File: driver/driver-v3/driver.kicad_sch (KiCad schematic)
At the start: 40 parts, among them J1 Conn_02x08_Odd_Even_Male, J2 Conn_02x08_Odd_Even_Female, J3 Conn_01x05, J4 Conn_01x03_Pin, J5 Conn_01x05, J6 Conn_01x03_Pin, U1 DRV8804PWP, U2 SN74HCS165DYYR, U3 DRV8804PWP

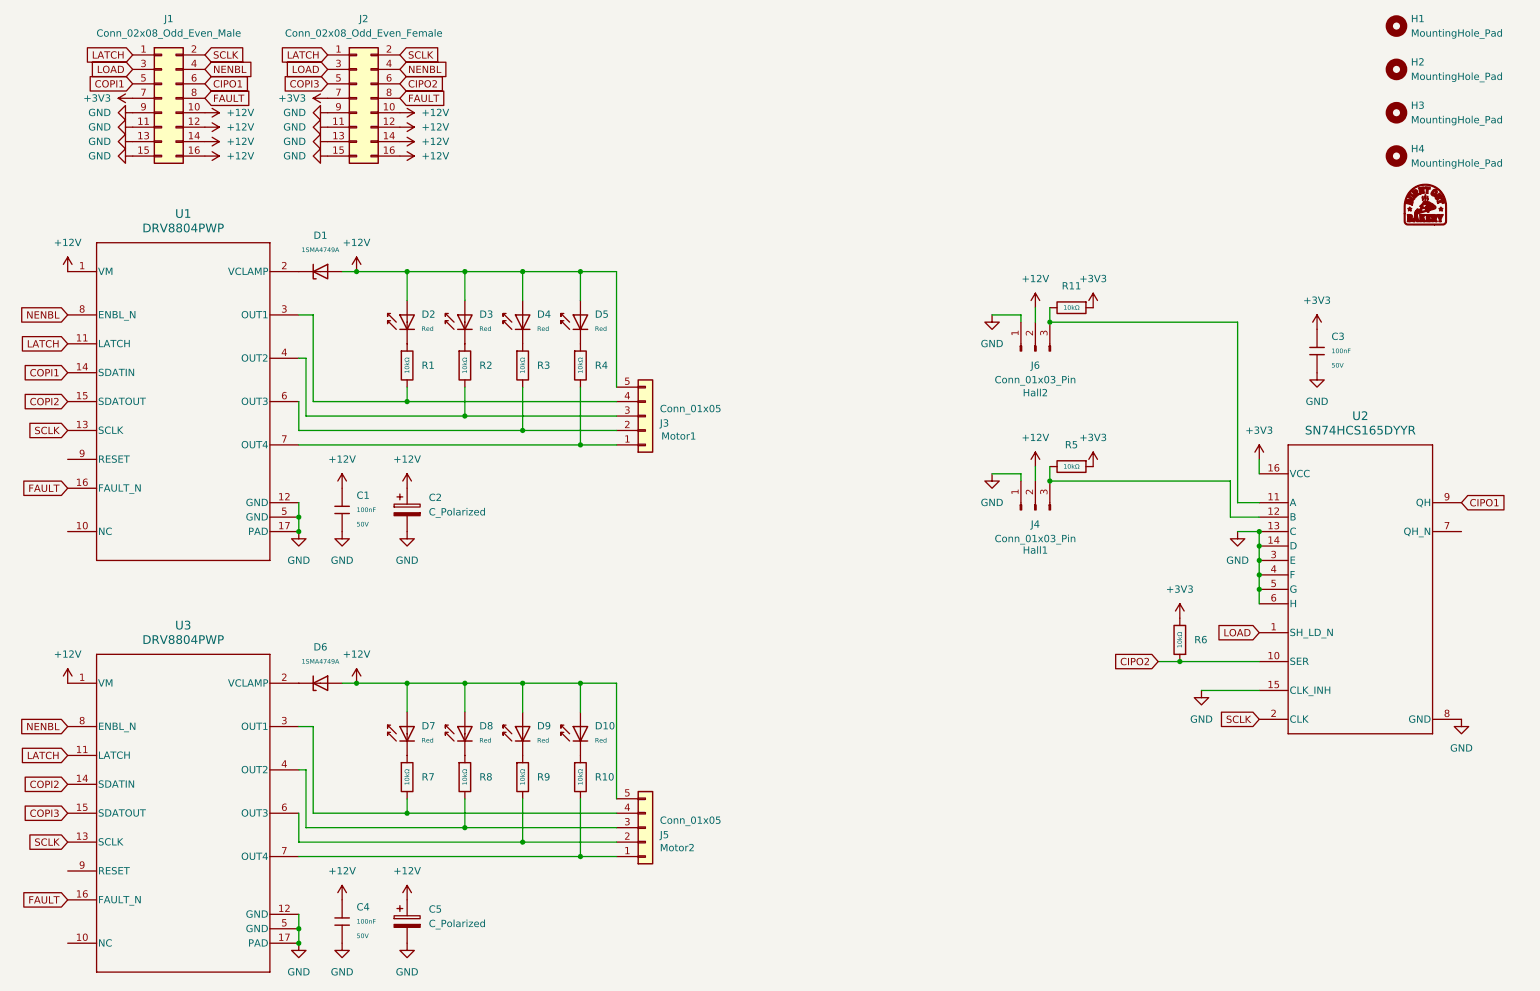
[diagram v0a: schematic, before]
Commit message: Optimize driver3 size and re-add spin test to firmware.
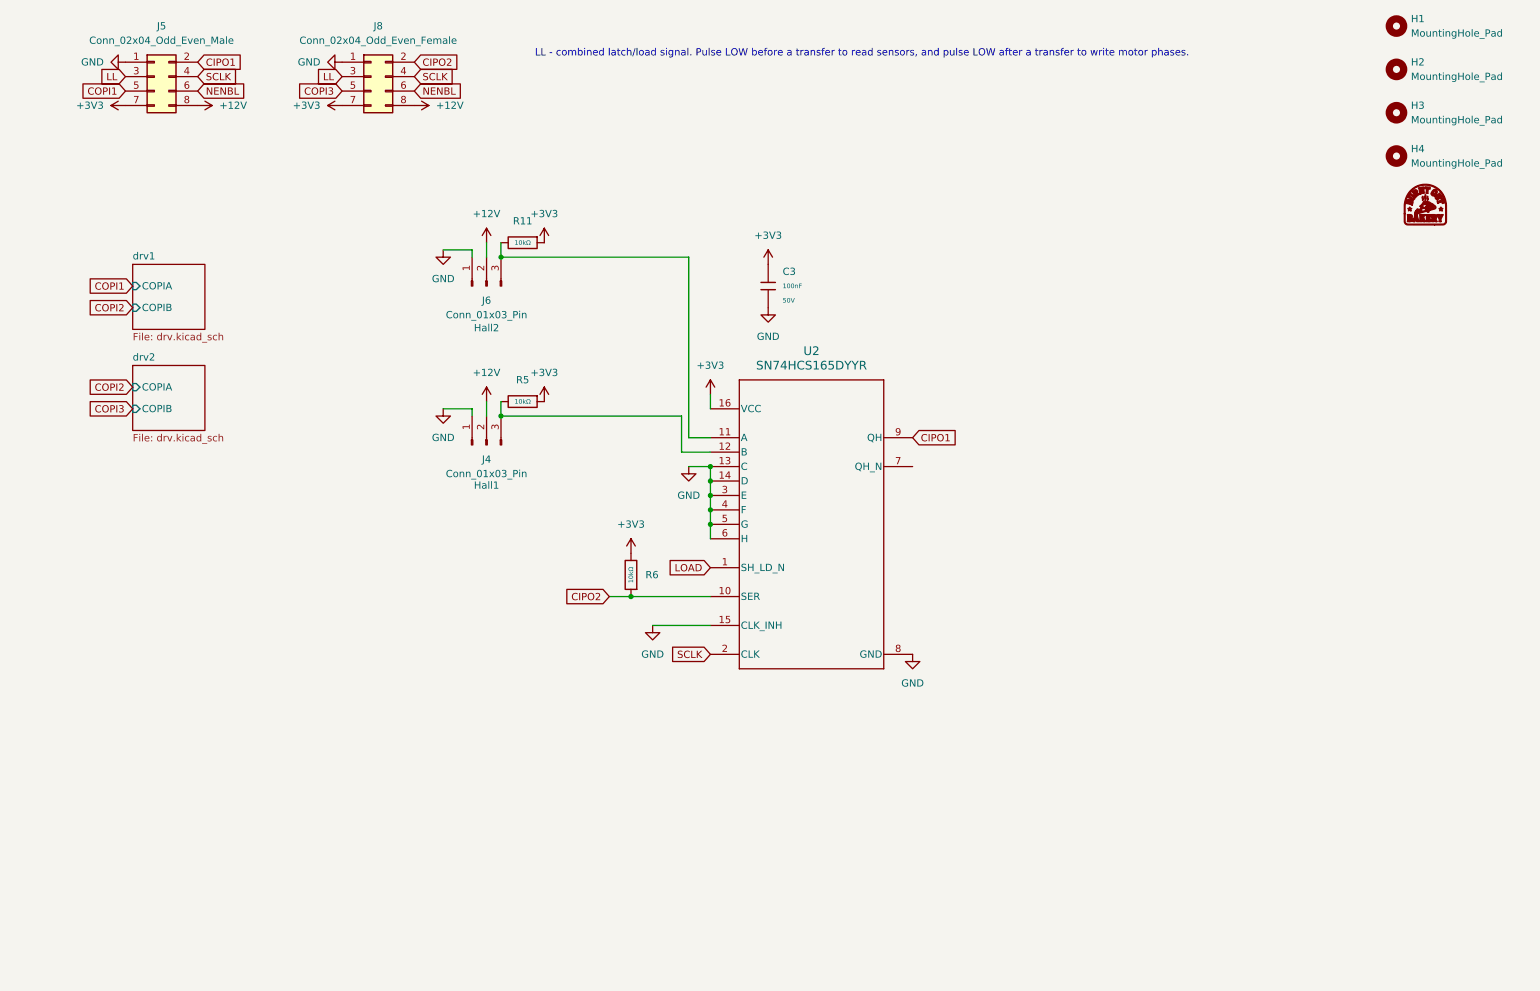
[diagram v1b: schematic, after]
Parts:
- removed C1, C4: 100nF, PCM_JLCPCB:C_0603, symbol PCM_JLCPCB-Capacitors:0603,100nF
- removed C2, C5: C_Polarized, Capacitor_SMD:CP_Elec_5x5.4, symbol Device:C_Polarized
- removed D1, D6: 1SMA4749A, PCM_JLCPCB:D_DO-214AC(SMA), symbol PCM_JLCPCB-Diodes:Zener,1SMA4749A
- removed D10, D2, D3, D4, D5, D7, D8, D9: Red, PCM_JLCPCB:D_0603, symbol PCM_JLCPCB-Diodes:LED,0603,Red
- removed J1: Conn_02x08_Odd_Even_Male, Connector_PinHeader_2.54mm:PinHeader_2x08_P2.54mm_Horizontal, symbol Connector_Generic:Conn_02x08_Odd_Even
- removed J2: Conn_02x08_Odd_Even_Female, Connector_PinSocket_2.54mm:PinSocket_2x08_P2.54mm_Horizontal, symbol Connector_Generic:Conn_02x08_Odd_Even
- removed J3, J5: Conn_01x05, Connector_JST:JST_XH_B5B-XH-A_1x05_P2.50mm_Vertical, symbol Connector_Generic:Conn_01x05
- removed R1, R10, R2, R3, R4, R7, R8, R9: 10kΩ, PCM_JLCPCB:R_0402, symbol PCM_JLCPCB-Resistors:0402,10kΩ
- removed U1, U3: DRV8804PWP, Package_SO:HTSSOP-16-1EP_4.4x5mm_P0.65mm_EP3.4x5mm_Mask3x3mm_ThermalVias, symbol ul_DRV8804PWP:DRV8804PWP
- added J5: Conn_02x04_Odd_Even_Male, Connector_PinHeader_2.54mm:PinHeader_2x04_P2.54mm_Horizontal, symbol Connector_Generic:Conn_02x04_Odd_Even
- added J8: Conn_02x04_Odd_Even_Female, Connector_PinSocket_2.54mm:PinSocket_2x04_P2.54mm_Horizontal, symbol Connector_Generic:Conn_02x04_Odd_Even
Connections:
- net +12V: now also J5.8 (Pin_8), J8.8 (Pin_8)
- net +3V3: now also J5.7 (Pin_7), J8.7 (Pin_7)
- net CIPO1: now also J5.2 (Pin_2)
- net CIPO2: now also J8.2 (Pin_2)
- net COPI1: now also J5.5 (Pin_5)
- net COPI3: now also J8.5 (Pin_5)
- net GND: now also J5.1 (Pin_1), J8.1 (Pin_1)
- net NENBL: now also J5.6 (Pin_6), J8.6 (Pin_6)
- net SCLK: now also J5.4 (Pin_4), J8.4 (Pin_4)
- new net LL: J5.3 (Pin_3), J8.3 (Pin_3)
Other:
- added sheet drv1 (drv.kicad_sch)
- added sheet drv2 (drv.kicad_sch)
- note added: "LL - combined latch/load signal. Pulse LOW before a transfer to read sensors, and pulse LOW after a transfer to write motor phases."
- moved on the sheet: C3, J4, J6, R11, R5, R6, U2
